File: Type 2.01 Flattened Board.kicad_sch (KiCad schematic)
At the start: 7 parts

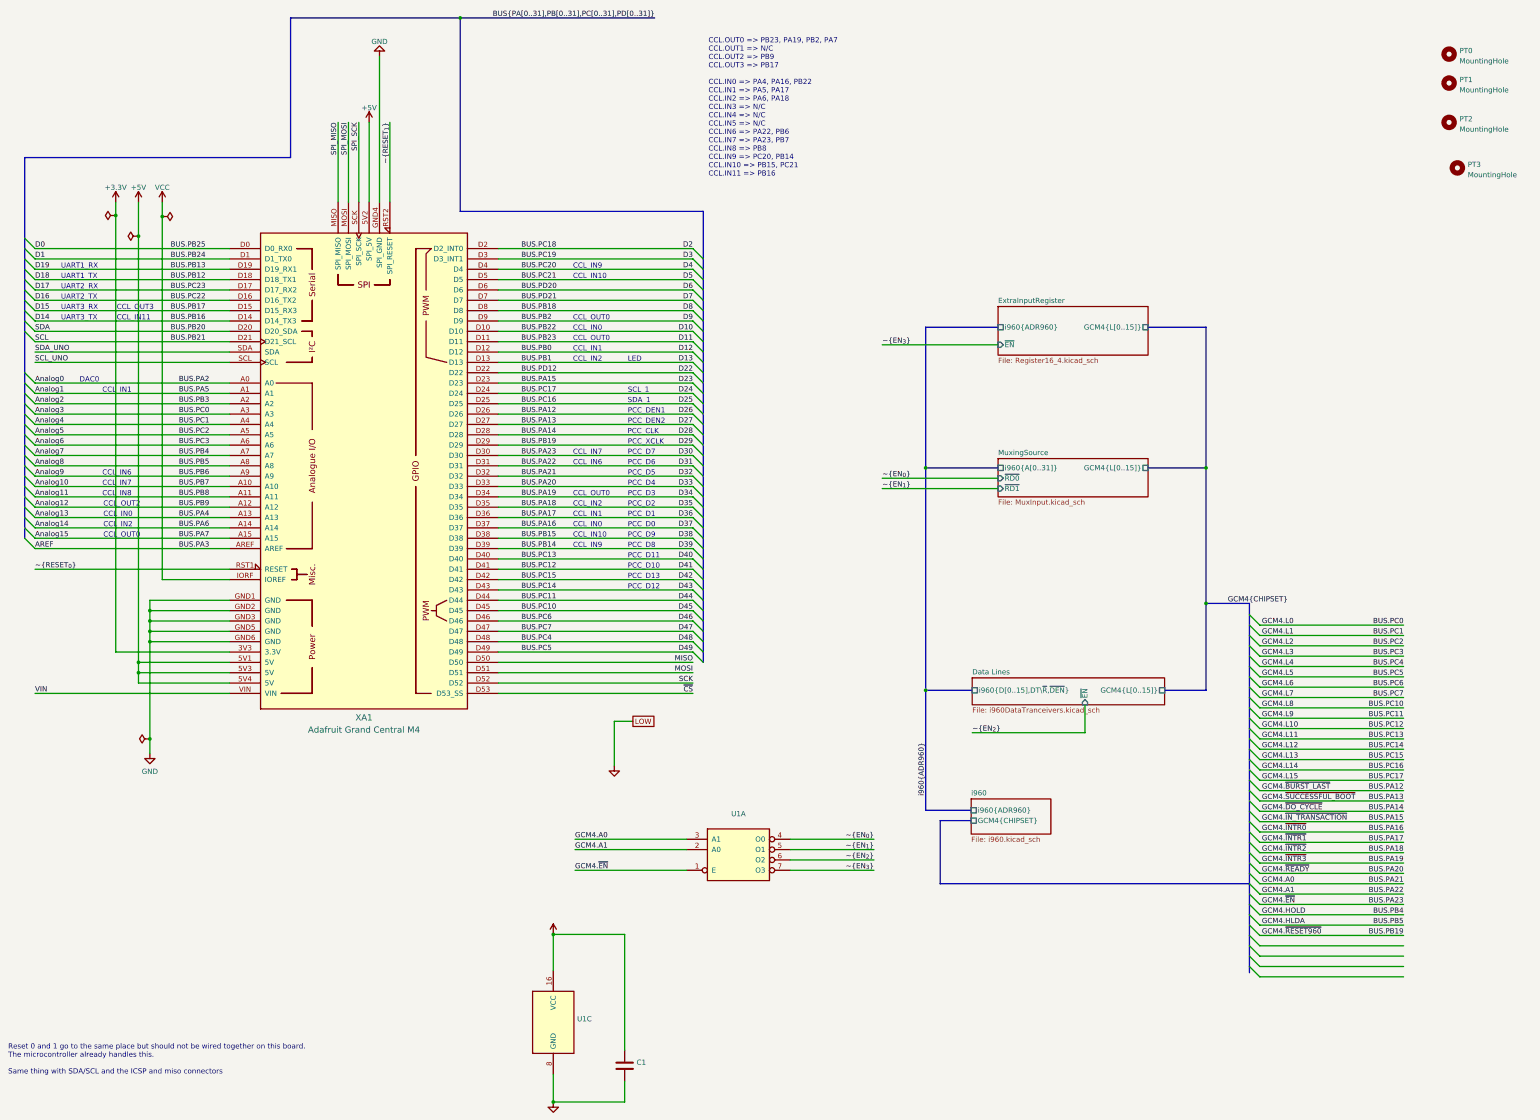
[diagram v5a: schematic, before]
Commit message: use the output enable lines on the latches and buffers to do direct logic level conversion
Save some chips in the process.
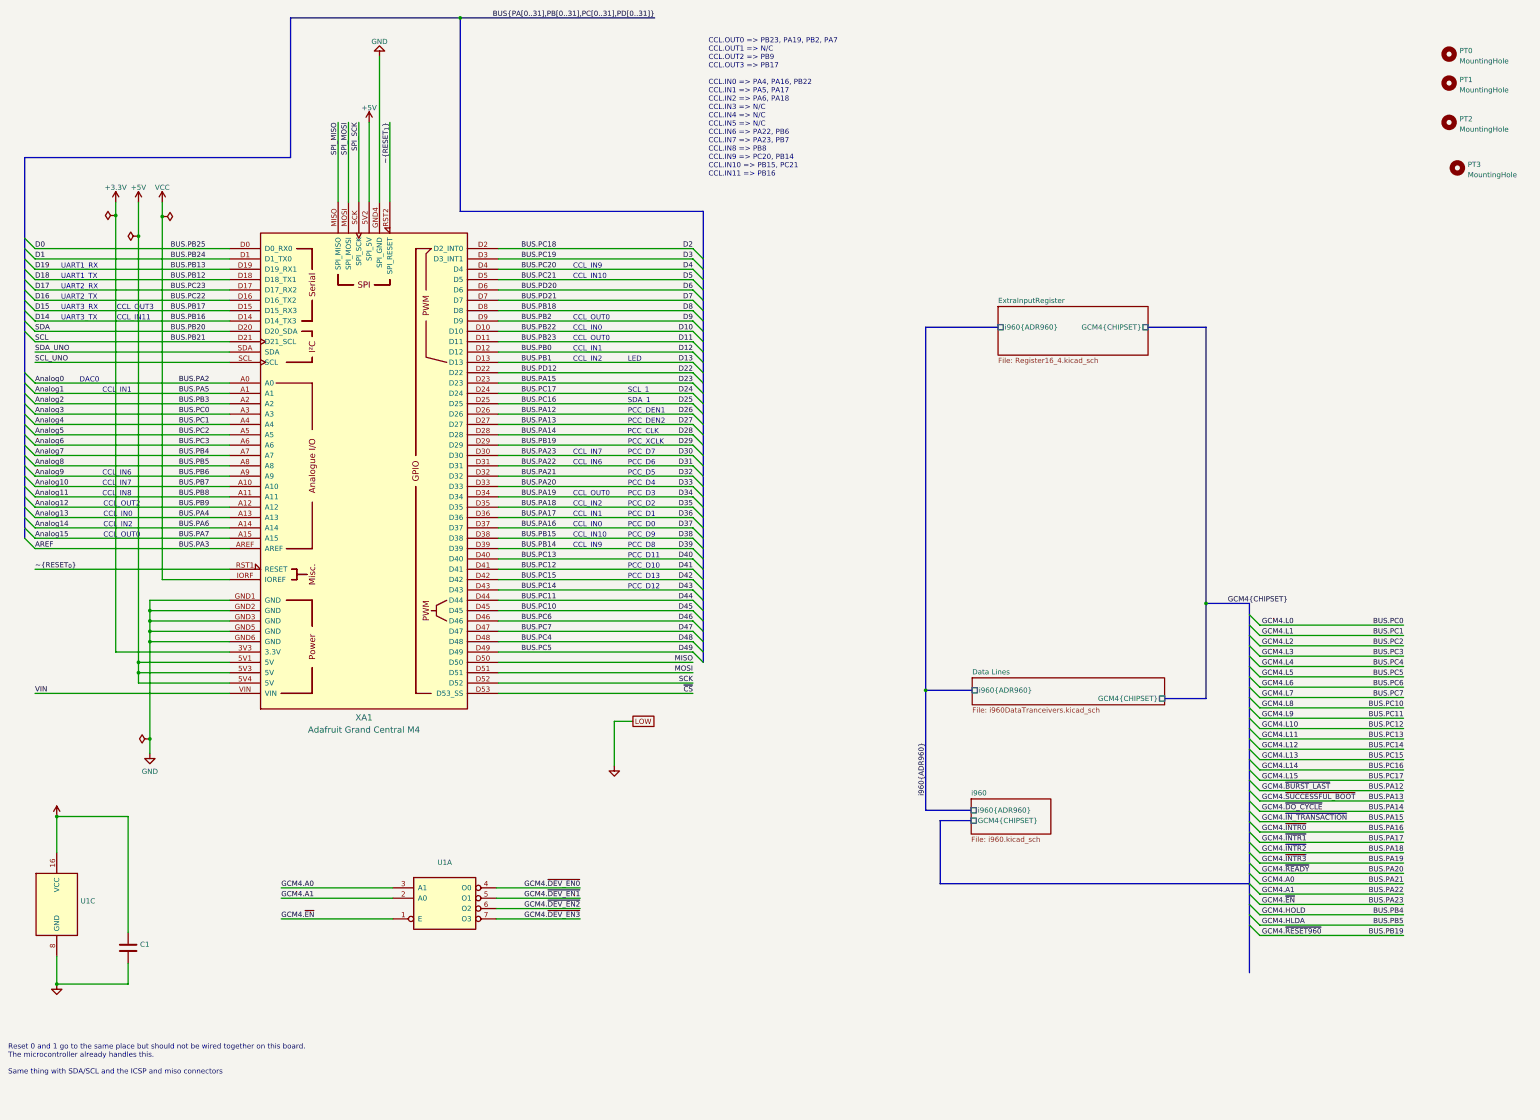
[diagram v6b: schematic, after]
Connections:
- net ~{EN_{0}} renamed GCM4.~{DEV_EN0}
- net ~{EN_{1}} renamed GCM4.~{DEV_EN1}
- net ~{EN_{2}} renamed GCM4.~{DEV_EN2}
- net ~{EN_{3}} renamed GCM4.~{DEV_EN3}
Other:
- removed sheet MuxingSource
- sheet Data Lines ports: added GCM4{CHIPSET}, i960{ADR960}; removed GCM4{L[0..15]}, i960{D[0..15],DT\~{R},~{DEN}}, ~{EN}
- sheet ExtraInputRegister ports: added GCM4{CHIPSET}; removed GCM4{L[0..15]}, ~{EN}
- moved on the sheet: C1, U1A, U1C

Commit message: Do a bulk update and fix all values
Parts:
- PT0, PT1, PT2, PT3: value MountingHole -> (none); footprint MountingHole:MountingHole_3.2mm_M3_ISO14580_Pad -> (none)
- XA1: value Adafruit Grand Central M4 -> (none); footprint Arduino_Alarm_Siren:Arduino_Mega2560_Shield -> (none)

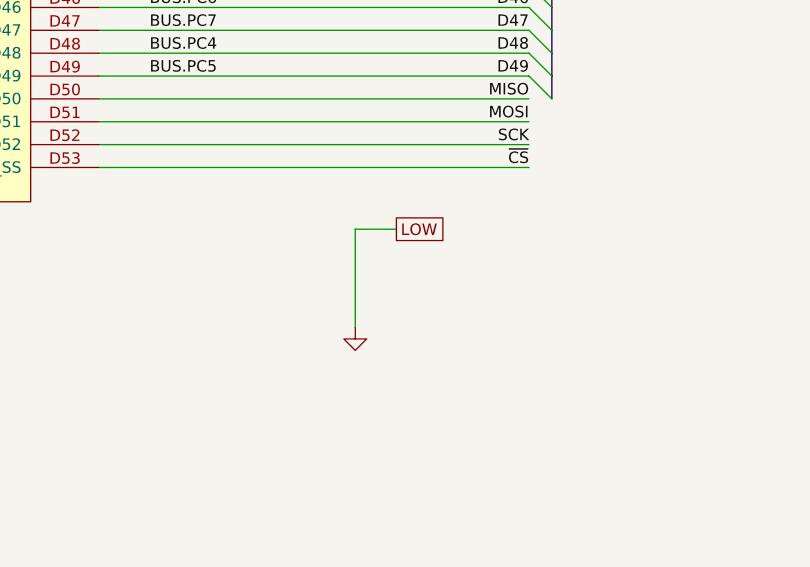
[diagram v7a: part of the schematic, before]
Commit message: Use individual resistors for better layout purposes
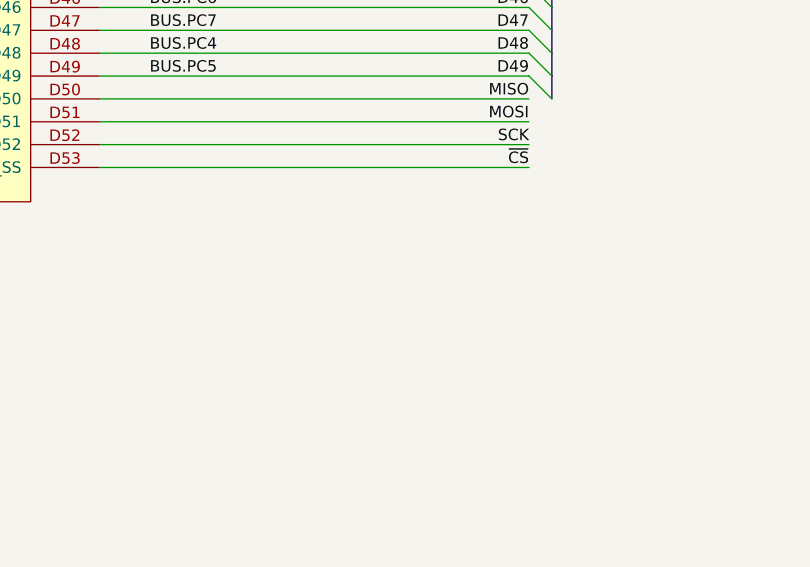
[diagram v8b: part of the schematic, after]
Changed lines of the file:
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@@
-    (stroke (width 0) (type default) (color 0 0 0 0))
-  )
-  (wire (pts (xy 172.72 189.23) (xy 168.148 189.23))
     (stroke (width 0) (type default) (color 0 0 0 0))
   )
@@
   )
   (bus (pts (xy 324.104 175.768) (xy 324.104 178.308))
-    (stroke (width 0) (type default) (color 0 0 0 0))
-  )
-  (wire (pts (xy 168.148 189.23) (xy 168.148 200.152))
     (stroke (width 0) (type default) (color 0 0 0 0))
   )
@@
   (label "BUS.PA20" (at 361.95 226.568 180)
     (effects (font (size 1.27 1.27)) (justify right bottom))
-  )
-  (global_label "LOW" (shape passive) (at 172.72 189.23 0) (fields_autoplaced)
-    (effects (font (size 1.27 1.27)) (justify left))
-    (property "Intersheet References" "${INTERSHEET_REFS}" (id 0) (at 178.8542 189.1506 0)
-      (effects (font (size 1.27 1.27)) (justify left) hide)
-    )
   )
   (symbol (lib_id "power:VCC") (at 31.242 212.598 0) (unit 1)
@@
     (pin "1")
   )
-  (symbol (lib_id "power:GND") (at 168.148 200.152 0) (unit 1)
-    (in_bom yes) (on_board yes) (fields_autoplaced)
-    (property "Reference" "#PWR06" (id 0) (at 168.148 206.502 0)
-      (effects (font (size 1.27 1.27)) hide)
-    )
-    (property "Value" "" (id 1) (at 168.148 204.5954 0))
-    (property "Footprint" "" (id 2) (at 168.148 200.152 0)
-      (effects (font (size 1.27 1.27)) hide)
-    )
-    (property "Datasheet" "" (id 3) (at 168.148 200.152 0)
-      (effects (font (size 1.27 1.27)) hide)
-    )
-    (pin "1")
-  )
   (symbol (lib_id "power:PWR_FLAG") (at 51.308 70.104 90) (unit 1)
     (in_bom yes) (on_board yes) (fields_autoplaced)
@@
       (reference "#PWR05") (unit 1) (value "+5V") (footprint "")
     )
-    (path "/edbfded8-58b0-4c33-ba55-66a325a1b8e4"
-      (reference "#PWR06") (unit 1) (value "GND") (footprint "")
+    (path "/cd4173d7-5549-43d9-b4b1-83989500a84c/948941d9-5990-454f-9b30-189af36f1623"
+      (reference "#PWR06") (unit 1) (value "+5V") (footprint "")
     )
     (path "/cd4173d7-5549-43d9-b4b1-83989500a84c/f2b8e171-5b62-402a-8228-906cadcfad9d"
@@
       (reference "J1") (unit 1) (value "Conn_01x05") (footprint "Connector_PinHeader_2.54mm:PinHeader_1x05_P2.54mm_Vertical")
     )
-    (path "/cd4173d7-5549-43d9-b4b1-83989500a84c/9b27769d-fd95-40b0-926b-936fc8d91675"
-      (reference "J2") (unit 1) (value "Conn_01x03") (footprint "Connector_PinHeader_2.54mm:PinHeader_1x03_P2.54mm_Vertical")
-    )
-    (path "/cd4173d7-5549-43d9-b4b1-83989500a84c/2b4df5a7-c8c5-44ae-9a36-2f3238cd3da8"
-      (reference "J3") (unit 1) (value "Conn_01x03") (footprint "Connector_PinHeader_2.54mm:PinHeader_1x03_P2.54mm_Vertical")
-    )
     (path "/cd4173d7-5549-43d9-b4b1-83989500a84c/15285a82-8026-4c1a-875d-764403da219c"
       (reference "J4") (unit 1) (value "Conn_02x03_Odd_Even") (footprint "Connector_IDC:IDC-Header_2x03_P2.54mm_Horizontal")
@@
       (reference "R1") (unit 1) (value "910") (footprint "Resistor_SMD:R_0805_2012Metric_Pad1.20x1.40mm_HandSolder")
     )
+    (path "/cd4173d7-5549-43d9-b4b1-83989500a84c/d06cbe01-ca73-4e56-9f09-e0aefe983993"
+      (reference "R2") (unit 1) (value "10k") (footprint "Resistor_SMD:R_0805_2012Metric_Pad1.20x1.40mm_HandSolder")
+    )
+    (path "/cd4173d7-5549-43d9-b4b1-83989500a84c/d19c34e0-8a9a-416a-b862-ad751fde4fb3"
+      (reference "R3") (unit 1) (value "10k") (footprint "Resistor_SMD:R_0805_2012Metric_Pad1.20x1.40mm_HandSolder")
+    )
     (path "/cd4173d7-5549-43d9-b4b1-83989500a84c/afad75f8-0ac4-4b1d-b080-f0ca6ba269a2"
       (reference "RN1") (unit 1) (value "R_Network12") (footprint "Resistor_THT:R_Array_SIP13")
@@
       (reference "U1") (unit 3) (value "74AHC139") (footprint "Package_SO:SOIC-16_3.9x9.9mm_P1.27mm")
     )
-    (path "/cd4173d7-5549-43d9-b4b1-83989500a84c/62ce1694-4177-4ca4-a31b-42e54da1e3e4"
-      (reference "U2") (unit 1) (value "74AHC244") (footprint "Package_DIP:DIP-20_W7.62mm_Socket")
-    )
-    (path "/cd4173d7-5549-43d9-b4b1-83989500a84c/d21f31ec-cd89-4c1b-b8fb-f121e369eb4b"
-      (reference "U3") (unit 1) (value "74AHC244") (footprint "Package_DIP:DIP-20_W7.62mm_Socket")
+    (path "/2d26b58a-1259-4cf5-aa8e-80f6b07f6859/7861ee13-f8ba-4e98-aafe-09acd8610749"
+      (reference "U2") (unit 1) (value "74AHC245") (footprint "Package_SO:SOIC-20W_7.5x12.8mm_P1.27mm")
+    )
+    (path "/2d26b58a-1259-4cf5-aa8e-80f6b07f6859/ae7d3d4a-243f-46ed-90cb-fdd443869fb6"
+      (reference "U3") (unit 1) (value "74AHC245") (footprint "Package_SO:SOIC-20W_7.5x12.8mm_P1.27mm")
+    )
+    (path "/cd4173d7-5549-43d9-b4b1-83989500a84c/331639a4-5c2a-4a3b-bfa9-42ccfdbb32e7"
+      (reference "U4") (unit 1) (value "74AHC245") (footprint "Package_SO:SOIC-20W_7.5x12.8mm_P1.27mm")
+    )
+    (path "/cd4173d7-5549-43d9-b4b1-83989500a84c/0fb12f6c-8388-431b-9389-d4531dca75d7"
+      (reference "U5") (unit 1) (value "74AHC245") (footprint "Package_SO:SOIC-20W_7.5x12.8mm_P1.27mm")
     )
     (path "/9e7b68f8-8caa-4a1d-85d2-3f3d0dd0043a/cf8e866e-7fd8-48bc-9cd1-0629363574e3"
@@
       (reference "U10") (unit 1) (value "74AHC138") (footprint "Package_SO:SOIC-16_3.9x9.9mm_P1.27mm")
     )
-    (path "/cd4173d7-5549-43d9-b4b1-83989500a84c/5dfa9718-b45b-409b-85c7-3dd9bb1e7c09"
-      (reference "U11") (unit 1) (value "74AHC244") (footprint "Package_DIP:DIP-20_W7.62mm_Socket")
-    )
-    (path "/2d26b58a-1259-4cf5-aa8e-80f6b07f6859/e7099e49-45b2-4d91-83f4-8a1a8eeecb05"
-      (reference "U12") (unit 1) (value "74AHC244") (footprint "Package_DIP:DIP-20_W7.62mm_Socket")
+    (path "/cd4173d7-5549-43d9-b4b1-83989500a84c/bc36a70a-0d40-4e22-ac37-b933b8938b31"
+      (reference "U11") (unit 1) (value "74AHC245") (footprint "Package_SO:SOIC-20W_7.5x12.8mm_P1.27mm")
+    )
+    (path "/cd4173d7-5549-43d9-b4b1-83989500a84c/c8d4d70f-3a8f-4a68-9c65-fc1ef32edd55"
+      (reference "U12") (unit 1) (value "74AHC245") (footprint "Package_SO:SOIC-20W_7.5x12.8mm_P1.27mm")
     )
     (path "/cd4173d7-5549-43d9-b4b1-83989500a84c/4c98d838-4530-4c37-a157-b3a85ef63936"
@@
       (reference "U19") (unit 1) (value "74AHC573") (footprint "Package_SO:SOIC-20W_7.5x12.8mm_P1.27mm")
     )
-    (path "/cd4173d7-5549-43d9-b4b1-83989500a84c/dc0a67ae-f826-4b28-bc64-86cf8c90b043"
-      (reference "U20") (unit 1) (value "74AHC244") (footprint "Package_DIP:DIP-20_W7.62mm_Socket")
-    )
-    (path "/2d26b58a-1259-4cf5-aa8e-80f6b07f6859/c58d427c-aec3-48b4-915f-b936c8e35e2f"
-      (reference "U21") (unit 1) (value "74AHC244") (footprint "Package_DIP:DIP-20_W7.62mm_Socket")
-    )
     (path "/2bd6b25f-a519-4224-8dd9-2e42d262ce2e"
